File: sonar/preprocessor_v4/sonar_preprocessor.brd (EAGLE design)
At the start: 130.8 x 50.8 mm, 184 parts, among them CON4 MOLEX_5566-2, U1 TEENSY_3.1_BASIC, U10 LT1117-5, U11 MMBT3904, U12 AD8336ACPZ-R7, U13 AD8336ACPZ-R7, U14 U14, U15 U15, U16 U16, U18 ISL21080DIH309Z-TK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

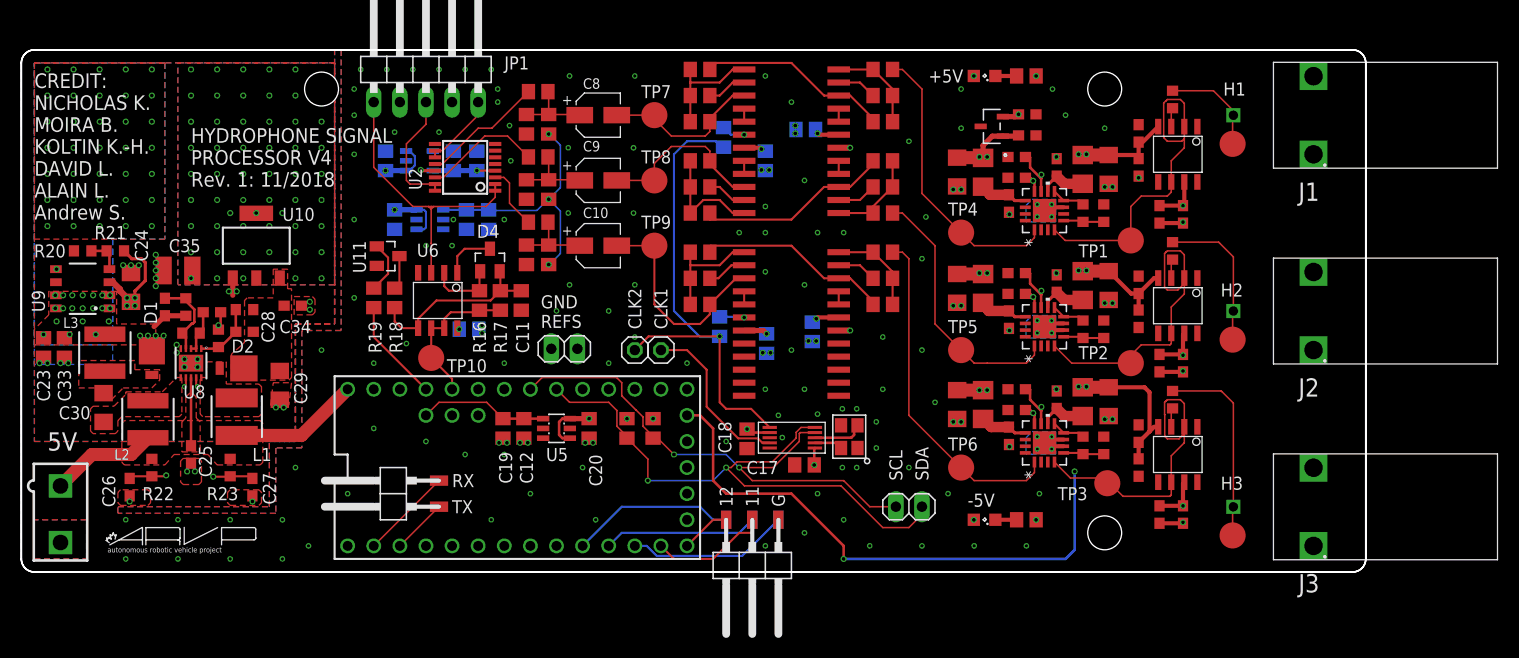
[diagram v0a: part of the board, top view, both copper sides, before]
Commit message: Changed BNC connectors from right-angle to straight such that the board is compatible with the old and new electronics tray designs. Modified BOM to reflect changes.
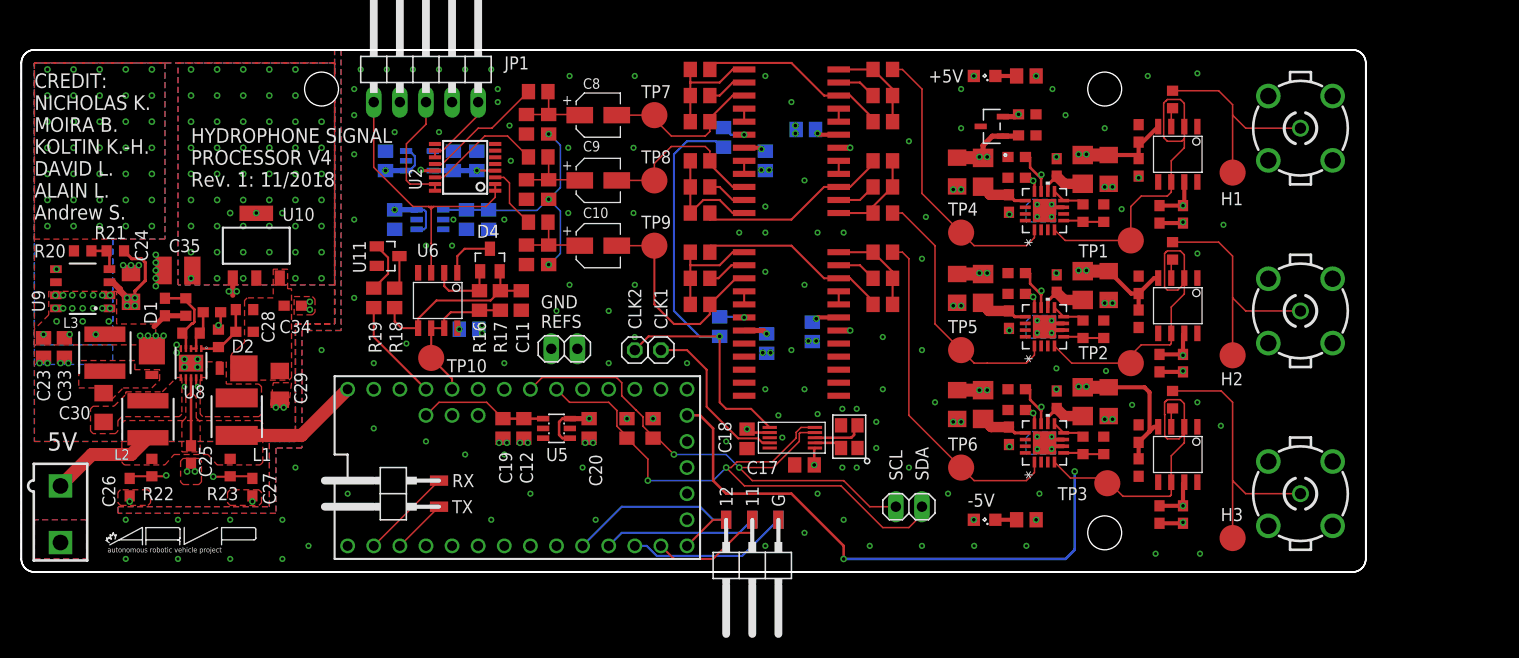
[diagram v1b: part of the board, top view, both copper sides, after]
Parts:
- J1, J2, J3: value (none) -> TE_5-1634503-1TE; device ARVP:CONN_BNC_R/A -> ARVP:TE_5-1634503-1
- moved J3 5.24 mm to (48.3, -41.9), turned to 270 degrees
- moved J2 4.02 mm to (48.3, -24.1)
- moved J1 2.84 mm to (48.3, -6.35)
- moved H1 2.79 mm to (41.7, -10.7)
- moved H2 1.52 mm to (41.7, -28.4)
- moved H3 0.25 mm to (41.7, -46.2)
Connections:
- net GND: now also J1.2, J1.3, J1.4, J1.5, J2.2, J2.3, J2.4, J2.5, J3.2, J3.3, J3.4, J3.5; no longer J1.GND1, J1.GND2\, J2.GND1, J2.GND2\, J3.GND1, J3.GND2\
- net N$18: now also J3.1; no longer J3.SIG
- net N$20: now also J2.1; no longer J2.SIG
- net N$23: now also J1.1; no longer J1.SIG
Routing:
- net N$23: track 9.98 -> 20.1 mm
- net N$20: track 14.6 -> 23.2 mm
- net N$18: track 19.3 -> 26.6 mm
- net GND: vias 192 -> 204
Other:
- board text removed: "Internal sensor board location (2"x2")"
- board text removed: "Torpedo board location (3"x2")"

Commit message: Added GND test point loop for oscilliscope ground probe and updated CAM files and schematica png.
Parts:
- added R35: RCT-0C, ARVP:RESC2012X65N
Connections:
- net GND: now also R35.1, R35.2
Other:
- board text added: "GND"

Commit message: JLCPCB didn't like where my origin was so I moved it :P
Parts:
- moved 25MHZ1 184.5 mm to (148.3, 76.8)
- moved C1 184.5 mm to (104.0, 104.8)
- moved C10 184.5 mm to (124.7, 96.5)
- moved C11 184.5 mm to (117.2, 91.2)
- moved C12 184.5 mm to (117.5, 78.7)
- moved C13 184.5 mm to (141.0, 104.8)
- moved C14 184.5 mm to (144.9, 107.8)
- moved C15 184.5 mm to (141.1, 87.0)
- moved C16 184.5 mm to (145.5, 88.1)
- moved C17 184.5 mm to (144.8, 75.2)
- moved C18 184.5 mm to (139.2, 77.7)
- moved C19 184.5 mm to (115.4, 78.7)
- moved C2 184.5 mm to (112.1, 88.4)
- moved C20 184.5 mm to (123.8, 78.7)
- moved C21 184.5 mm to (169.3, 104.1)
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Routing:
- net INPUT2: track 30.8 -> 20.2 mm
